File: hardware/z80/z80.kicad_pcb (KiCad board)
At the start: 2 copper layers, 99.1 x 99.1 mm, 13 parts, among them J1 nuMezzanine_4x34, U1 Z84C0008PEG

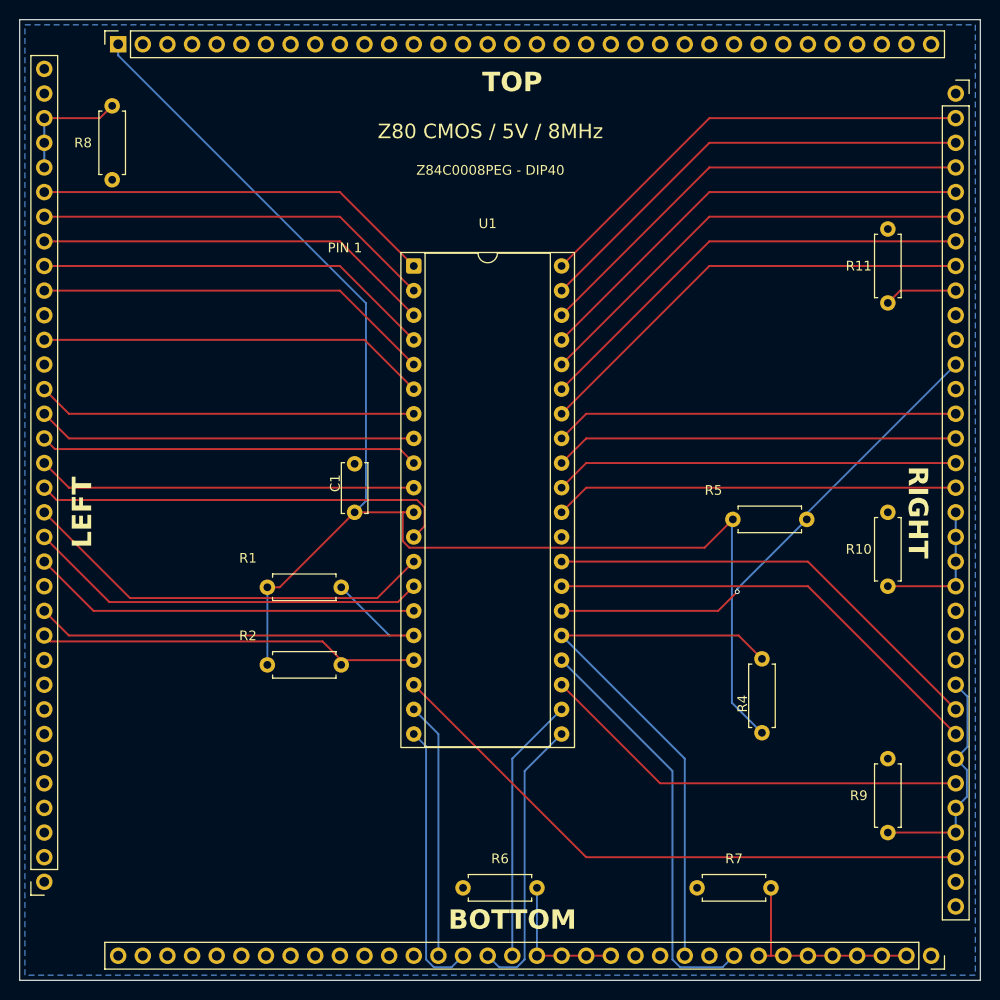
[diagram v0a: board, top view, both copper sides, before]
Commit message: Update mainboard to revision 2
Add an additional 8 bidirectional channels
Replace SPI PSRAM with hyperram
Remove LEDs
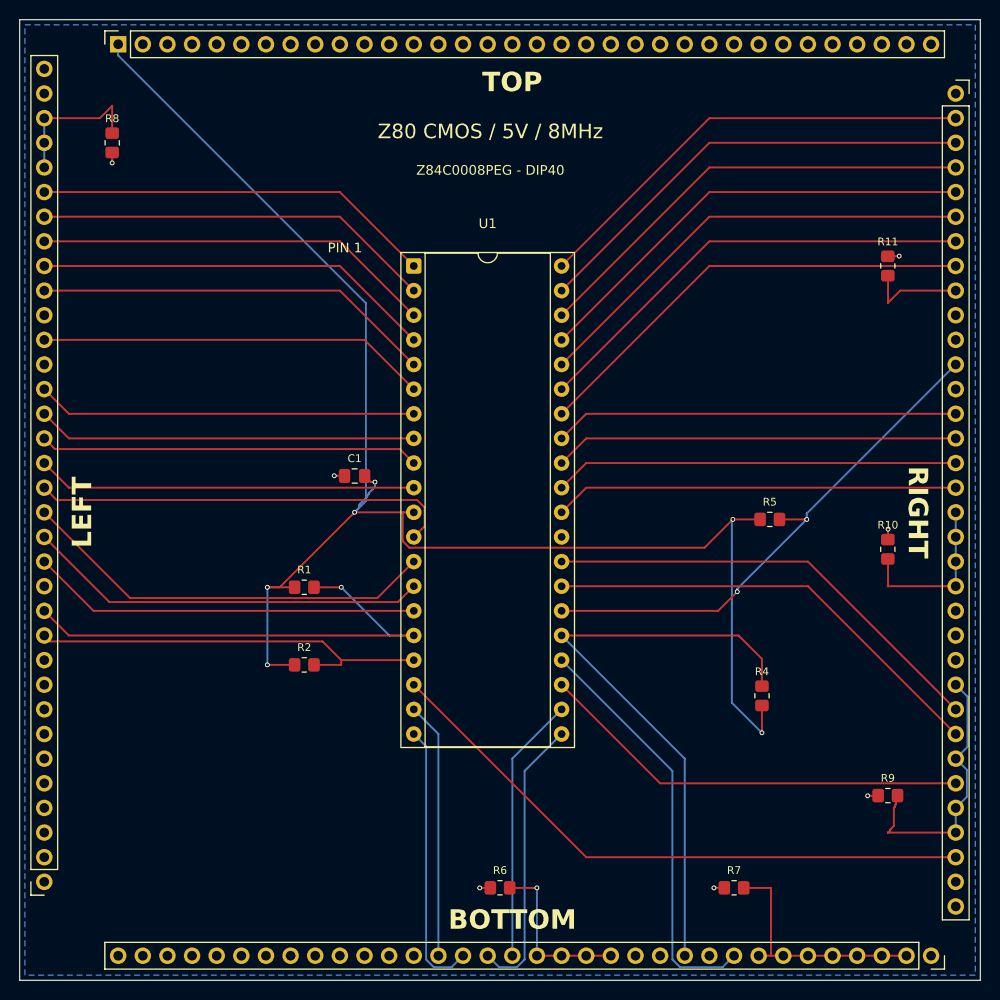
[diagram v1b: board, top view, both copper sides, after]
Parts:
- C1: footprint Capacitor_THT:C_Disc_D5.0mm_W2.5mm_P5.00mm -> Capacitor_SMD:C_0805_2012Metric_Pad1.18x1.45mm_HandSolder
- R1, R10, R11, R2, R4, R5, R6, R7, R8, R9: footprint Resistor_THT:R_Axial_DIN0207_L6.3mm_D2.5mm_P7.62mm_Horizontal -> Resistor_SMD:R_0805_2012Metric_Pad1.20x1.40mm_HandSolder
- moved R1 3.81 mm to (130.8, 105.0)
- moved R10 3.81 mm to (191.0, 101.1)
- moved R11 3.81 mm to (191.0, 71.9)
- moved R2 3.81 mm to (130.8, 113.0)
- moved R4 3.81 mm to (178.0, 116.2)
- moved R5 3.81 mm to (178.8, 98.0)
- moved R6 3.81 mm to (151.0, 136.0)
- moved R7 3.81 mm to (175.1, 136.0)
- moved R8 3.81 mm to (111.0, 59.2)
- moved R9 3.81 mm to (191.0, 126.5), turned to 180 degrees
- moved C1 3.75 mm to (136.0, 93.5), turned to 180 degrees
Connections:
- net /BY renamed /BX2
- net /LX renamed /LX1
- net /LY renamed /LX2
- net /RX renamed /RX1
- J1 pad 10: GND -> unconnected-(J1A-TX3-Pad10)
- J1 pad 102: unconnected-(J1E-NC-Pad102) -> GND
- J1 pad 112: GND -> unconnected-(J1B-LX3-Pad112)
- J1 pad 115: GND -> unconnected-(J1B-LX0-Pad115)
- J1 pad 13: GND -> unconnected-(J1A-TX0-Pad13)
- J1 pad 136: unconnected-(J1E-NC-Pad136) -> GND
- J1 pad 44: GND -> unconnected-(J1D-RX3-Pad44)
- J1 pad 47: GND -> unconnected-(J1D-RX0-Pad47)
- J1 pad 78: GND -> unconnected-(J1C-BX3-Pad78)
- J1 pad 81: GND -> unconnected-(J1C-BX0-Pad81)
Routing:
- net /VCC_TL: track 147.5 -> 164.0 mm, vias 0 -> 6
- net GND: track 0.00 -> 7.81 mm, vias 0 -> 7
- net /R0_UNUSED: track 24.2 -> 28.5 mm
- net /R2_UNUSED: track 7.53 -> 10.4 mm
- net /B2_UNUSED: track 22.2 -> 25.1 mm
- net /R1_UNUSED: track 14.6 -> 17.5 mm
- net /BX2: track 59.9 -> 62.8 mm
- net /L0_UNUSED: track 12.6 -> 15.4 mm
- net /RX1: track 51.7 -> 54.5 mm, vias 1 -> 2
- net /LX2: track 39.6 -> 42.5 mm
- net /LX1: track 48.7 -> 51.5 mm, vias 0 -> 1
- net /B1_UNUSED: track 14.6 -> 17.4 mm, vias 0 -> 1
